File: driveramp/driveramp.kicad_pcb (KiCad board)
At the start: 2 copper layers, 109 x 79 mm, 62 parts, among them J1 SMA, J2 SMA, P1 FAULT, P2 CONN_2, T1 MABA-011002, T2 2x Fair-Rite 2843006802, coax, U1 LM2936HVBMA-5.0, U2 MRFE6VP100H, U3 LM317HV

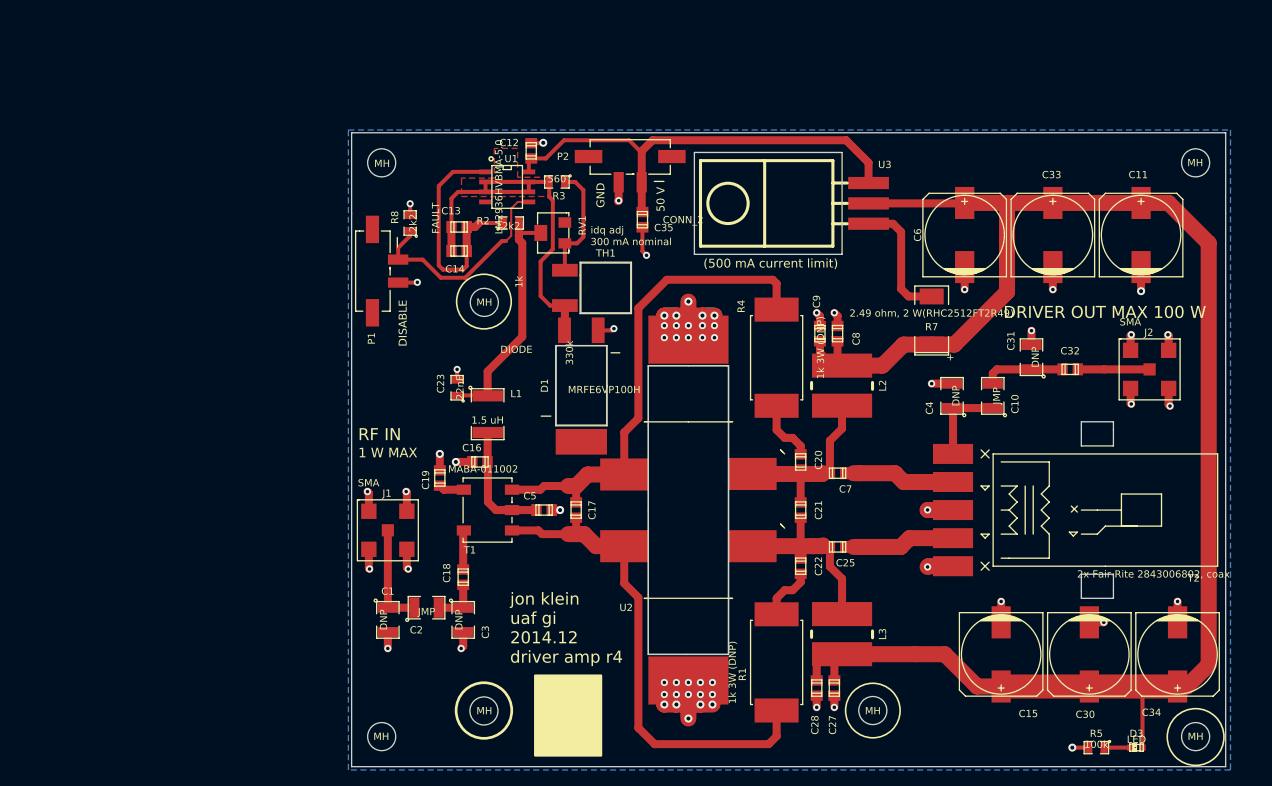
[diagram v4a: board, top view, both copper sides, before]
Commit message: added libraries for r5 driver amp - connectors, mounting holes. changed switch due to availability
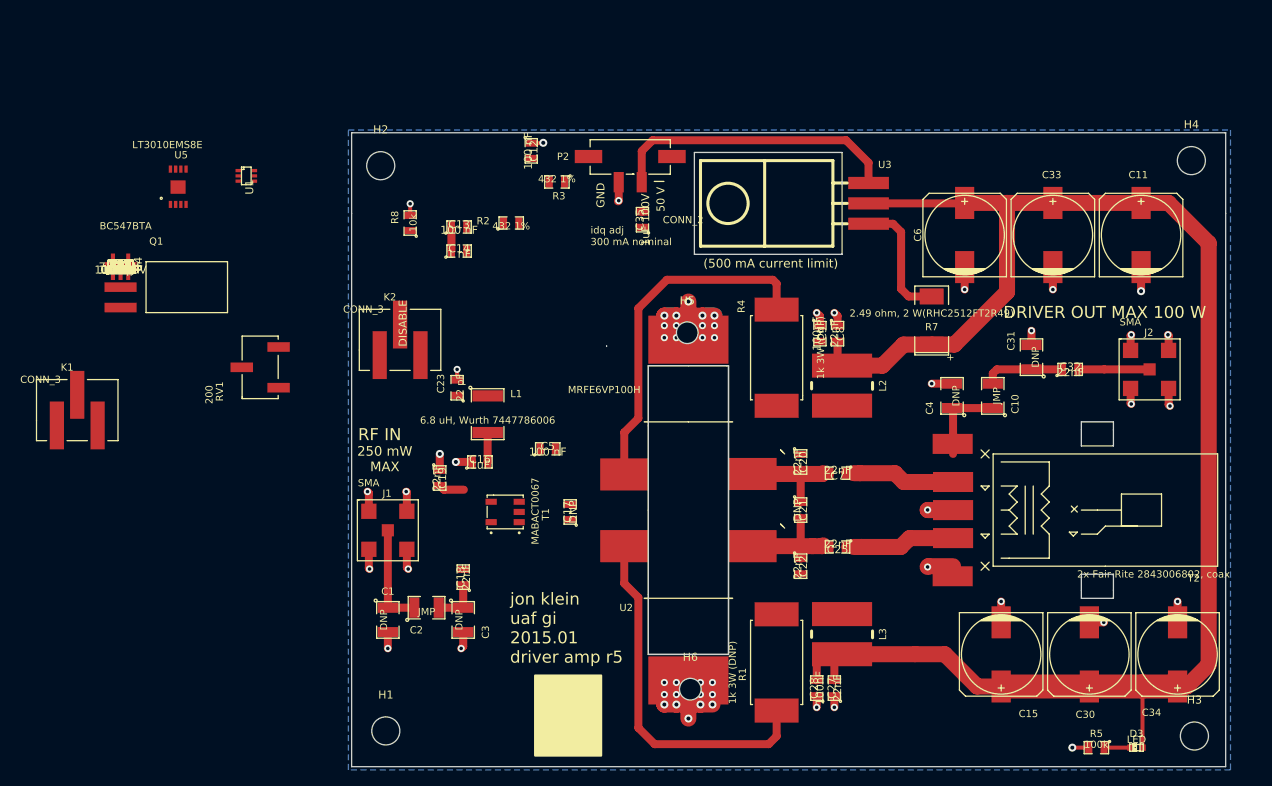
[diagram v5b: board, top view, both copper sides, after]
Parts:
- removed D1: DIODE, local:DUAL_DIODE
- removed MH (x7): MountingHole_3-5mm_RevA_Date21Jun2010, Mounting_Holes:MountingHole_3-5mm
- removed P1: FAULT, local:2-1445053-2
- removed TH1: 330k, local:NTC_HSMOUNT
- added C24: 100 pF, SMD_Packages:SMD-0805, F.Cu at (47.2, 79.7)
- added C26: 10 nF, SMD_Packages:SMD-0805, F.Cu at (47.2, 79.7)
- added C29: 1000 pF, SMD_Packages:SMD-0805, F.Cu at (47.2, 79.7)
- added C36, C39: 100 nF, SMD_Packages:SMD-0805, F.Cu at (47.2, 79.7)
- added C37, C38: 1uF, SMD_Packages:SMD-0805, F.Cu at (47.2, 79.7)
- added C40: 1uF 100V, SMD_Packages:SMD-0805, F.Cu at (47.2, 79.7)
- added H1: MOUNTING_HOLE, Mounting_Holes:MountingHole_3-5mm, F.Cu at (80.3, 137.5)
- added H2: MOUNTING_HOLE, Mounting_Holes:MountingHole_3-5mm, F.Cu at (79.6, 67.1)
- added H3: MOUNTING_HOLE, Mounting_Holes:MountingHole_3-5mm, F.Cu at (181.1, 138.2)
- added H4: MOUNTING_HOLE, Mounting_Holes:MountingHole_3-5mm, F.Cu at (180.7, 66.4)
- added H5: MOUNTING_HOLE, Mounting_Holes:MountingHole_2-7mm, F.Cu at (117.9, 87.9)
- added H6: MOUNTING_HOLE, Mounting_Holes:MountingHole_2-7mm, F.Cu at (118.2, 132.3)
- added K1: CONN_3, localconn:3-647166-3, F.Cu at (41.8, 97.5)
- added K2: CONN_3, localconn:3-647166-3, F.Cu at (82.0, 88.8)
- added Q1: BC547BTA, local:TO92SMDSENSE, F.Cu at (47.2, 79.7)
- added R10: 2k 1%, SMD_Packages:SMD-0603, F.Cu at (47.2, 79.7)
- added R11: 1.1k 1%, SMD_Packages:SMD-0603, F.Cu at (47.2, 79.7)
- added R12: 5.11k 1%, SMD_Packages:SMD-0603, F.Cu at (47.2, 79.7)
- added R13: 909 1%, SMD_Packages:SMD-0603, F.Cu at (47.2, 79.7)
- added R14: 10k 1%, SMD_Packages:SMD-0603, F.Cu at (47.2, 79.7)
- added R15: 1.5, SMD_Packages:SMD-0603, F.Cu at (47.2, 79.7)
- added R16: 5.1, SMD_Packages:SMD-0603, F.Cu at (47.2, 79.7)
- added R17, R18: DNP, SMD_Packages:SMD-0805, F.Cu at (47.2, 79.7)
- added R19: 20, SMD_Packages:SMD-0603, F.Cu at (47.2, 79.7)
- added R20: 52.3K 1%, SMD_Packages:SMD-0603, F.Cu at (47.2, 79.7)
- added R21: 10K 1%, SMD_Packages:SMD-0603, F.Cu at (47.2, 79.7)
- added R22: 10k, SMD_Packages:SMD-0603, F.Cu at (47.2, 79.7)
- added R23: 6.2 k, SMD_Packages:SMD-0603, F.Cu at (47.2, 79.7)
- added R6: 75 1%, SMD_Packages:SMD-0603, F.Cu at (47.2, 79.7)
- added R9: 9.1k, SMD_Packages:SMD-0603, F.Cu at (47.2, 79.7)
- added U4: 7321MF, SMD_Packages:SOT-23-5, F.Cu at (47.2, 79.7)
- added U5: LT3010EMS8E, local:MSOP8-EP, F.Cu at (54.4, 69.7)
- C12: value 100nF 50V -> 100 nF; footprint Capacitors_SMD:c_0805 -> SMD_Packages:SMD-0805
- C13: value 2.2uF -> 100 nF; footprint Capacitors_SMD:c_0805 -> SMD_Packages:SMD-0805
- C14: value 22nF -> 1 nF; footprint Capacitors_SMD:c_0805 -> SMD_Packages:SMD-0805
- C16: value 100nF -> 1uF; footprint Capacitors_SMD:c_0805 -> SMD_Packages:SMD-0805
- C17, C18, C19, C20, C21, C22, C25, C27, C28, C32, C35, C7, C8, C9: footprint Capacitors_SMD:c_0805 -> SMD_Packages:SMD-0805
- C23: value 22nF -> 22 pF
- C5: value 22nF -> 100 nF; footprint Capacitors_SMD:c_0805 -> SMD_Packages:SMD-0805
- L1: value 1.5 uH -> 6.8 uH, Wurth 7447786006
- R2: value 2k2 -> 432 1%
- R3: value 560 -> 432 1%
- R8: value 2k2 -> 10k
- RV1: value 1k -> 200; footprint local:POT_SMD -> local:3269W
- T1: value MABA-011002 -> MABACT0067; footprint local:MABA-01002 -> local:SM-22
- U1: value LM2936HVBMA-5.0 -> DG9411; footprint SOIC_Packages:SOIC-8_N -> Transistors_SMD:sc70-6
- moved RV1 40.1 mm to (64.6, 92.2)
- moved U1 32.6 mm to (62.9, 68.3)
- moved C5 7.65 mm to (100.5, 102.4), turned to 0 degrees
- moved T1 3.91 mm to (96.9, 110.2)
- moved C17 0.79 mm to (103.3, 110.2), turned to 90 degrees
- turned C32 to 0 degrees
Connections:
- C12 pad 1: /Vconn -> Net-(C12-Pad1)
- C13 pad 2: Net-(C13-Pad2) -> GND
- C14 pad 1: Net-(C13-Pad1) -> Net-(C14-Pad1)
- C14 pad 2: Net-(C13-Pad2) -> GND
- C23 pad 1: Net-(C23-Pad1) -> Net-(C14-Pad1)
- C5 pad 1: Net-(C16-Pad1) -> Net-(C5-Pad1)
- L1 pad 1: Net-(C23-Pad1) -> /Vconn
- L1 pad 2: Net-(C16-Pad1) -> Net-(C40-Pad1)
- R2 pad 1: Net-(C13-Pad1) -> +8V
- R2 pad 2: Net-(C23-Pad1) -> Net-(R2-Pad2)
- R3 pad 1: Net-(R3-Pad1) -> Net-(R2-Pad2)
- R3 pad 2: Net-(C13-Pad2) -> Net-(R3-Pad2)
- R8 pad 1: Net-(P1-Pad1) -> GND
- R8 pad 2: GND -> Net-(R8-Pad2)
- RV1 pad 1: Net-(R3-Pad1) -> Net-(R2-Pad2)
- RV1 pad 2: Net-(C23-Pad1) -> Net-(R10-Pad2)
- RV1 pad 3: (no net) -> Net-(R3-Pad2)
- T1 pad 1: Net-(C17-Pad1) -> Net-(C17-Pad2)
- T1 pad 2: Net-(C16-Pad1) -> Net-(R17-Pad2)
- T1 pad 3: Net-(C17-Pad2) -> Net-(C17-Pad1)
- U1 pad 1: Net-(C13-Pad1) -> Net-(R8-Pad2)
- U1 pad 2: Net-(C13-Pad2) -> Net-(C5-Pad1)
- U1 pad 3: Net-(C13-Pad2) -> GND
- U1 pad 4: (no net) -> Net-(R15-Pad2)
- U1 pad 5: Net-(P1-Pad1) -> Net-(R16-Pad2)
- U1 pad 6: Net-(C13-Pad2) -> Net-(C14-Pad1)
- U2 pad 1: Net-(C17-Pad2) -> (no net)
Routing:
- net Net-(C13-Pad2): track 48.7 -> 0.00 mm
- net Net-(C23-Pad1): track 30.4 -> 0.00 mm
- net Net-(P1-Pad1): track 27.4 -> 0.00 mm
- net Net-(C13-Pad1): track 30.1 -> 3.00 mm
- net /Vconn: track 61.0 -> 36.5 mm
- net Net-(C17-Pad2): track 64.0 -> 43.6 mm
- net Net-(C17-Pad1): track 62.9 -> 45.1 mm
- net Net-(R3-Pad1): track 14.6 -> 0.00 mm
- net Net-(C16-Pad1): track 15.2 -> 2.05 mm, vias 0 -> 1
- net Net-(C21-Pad1): track 30.1 -> 18.6 mm
- net GND: track 203.1 -> 193.4 mm, vias 65 -> 52
- net VDD: track 209.9 -> 200.7 mm, vias 0 -> 4
- net Net-(C25-Pad2): track 14.9 -> 7.47 mm
- net Net-(C7-Pad2): track 14.7 -> 7.39 mm
- net Net-(C22-Pad1): track 6.88 -> 0.00 mm
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- removed copper zone on F.Cu, net Net-(C13-Pad2)
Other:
- outline, holes or cut-outs redrawn
- board text added: "250 mW MAX"
- board text added: "jon klein uaf gi 2015.01 driver amp r5"
- board text removed: "1 W MAX"
- board text removed: "Attach VHS-95 heatsink to bottom"
- board text removed: "jon klein uaf gi 2014.12 driver amp r4"

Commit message: layout on r5
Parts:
- added L4: FERRITE BEAD, SMD_Packages:SMD-0805, F.Cu at (100.5, 67.7)
- R19: footprint SMD_Packages:SMD-0603 -> SMD_Packages:SMD-0805
- R2, R3, R8: footprint SMD_Packages:SM0805 -> SMD_Packages:SMD-0603
- moved Q1 62.8 mm to (109.9, 83.7), turned to 270 degrees
- moved R13 62.2 mm to (109.3, 80.1), turned to 180 degrees
- moved R12 58.4 mm to (105.5, 80.1), turned to 180 degrees
- moved R11 57.7 mm to (104.8, 76.8), turned to 90 degrees
- moved C29 55.9 mm to (99.4, 99.4), turned to 270 degrees
- moved R17 55.1 mm to (99.8, 96.0)
- moved R14 54.8 mm to (102.0, 80.1), turned to 180 degrees
- moved C24 53.9 mm to (97.3, 99.4), turned to 270 degrees
- moved R19 53.5 mm to (100.6, 83.6), turned to 270 degrees
- moved R22 52.6 mm to (98.3, 67.4), turned to 90 degrees
- moved R16 51.9 mm to (96.4, 96.0), turned to 180 degrees
- moved R18 51.4 mm to (98.4, 83.6), turned to 90 degrees
- moved C40 50.5 mm to (95.4, 64.6), turned to 180 degrees
- moved R15 49.9 mm to (93.3, 98.7)
- moved C36 47.5 mm to (94.4, 85.6), turned to 270 degrees
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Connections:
- L1 pad 1: /Vconn -> Net-(L1-Pad1)
- L1 pad 2: Net-(C40-Pad1) -> Net-(L1-Pad2)
- R17 pad 2: Net-(R17-Pad2) -> Net-(L1-Pad1)
- R19 pad 1: Net-(R17-Pad2) -> Net-(C16-Pad1)
- R19 pad 2: Net-(C16-Pad1) -> Net-(L1-Pad1)
- T1 pad 2: Net-(R17-Pad2) -> Net-(L1-Pad2)
- U2 pad 1: (no net) -> Net-(C17-Pad2)
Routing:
- net +8V: track 0.00 -> 72.3 mm, vias 0 -> 5
- net GND: track 193.4 -> 156.3 mm, vias 52 -> 70
- net Net-(L1-Pad1): track 0.00 -> 23.8 mm
- net Net-(C13-Pad1): track 3.00 -> 26.0 mm
- net Net-(K2-Pad2): track 0.00 -> 22.1 mm
- net Net-(C14-Pad1): track 0.00 -> 20.9 mm
- net /Vconn: track 36.5 -> 57.0 mm
- net Net-(C16-Pad1): track 2.05 -> 17.7 mm, vias 1 -> 2
- net Net-(C17-Pad1): track 45.1 -> 60.3 mm
- net Net-(C17-Pad2): track 43.6 -> 58.0 mm
- net Net-(C21-Pad1): track 18.6 -> 30.3 mm
- net Net-(C12-Pad1): track 1.52 -> 10.3 mm, vias 1 -> 0
- net Net-(C22-Pad1): track 0.00 -> 7.44 mm
- net Net-(C25-Pad2): track 7.47 -> 14.9 mm
- net Net-(C7-Pad2): track 7.39 -> 14.7 mm
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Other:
- outline, holes or cut-outs redrawn
- net class Default: clearance 0.254 -> 0.18
- rule trace_clearance: 0.254 -> 0.18
- board text added: "T/R"

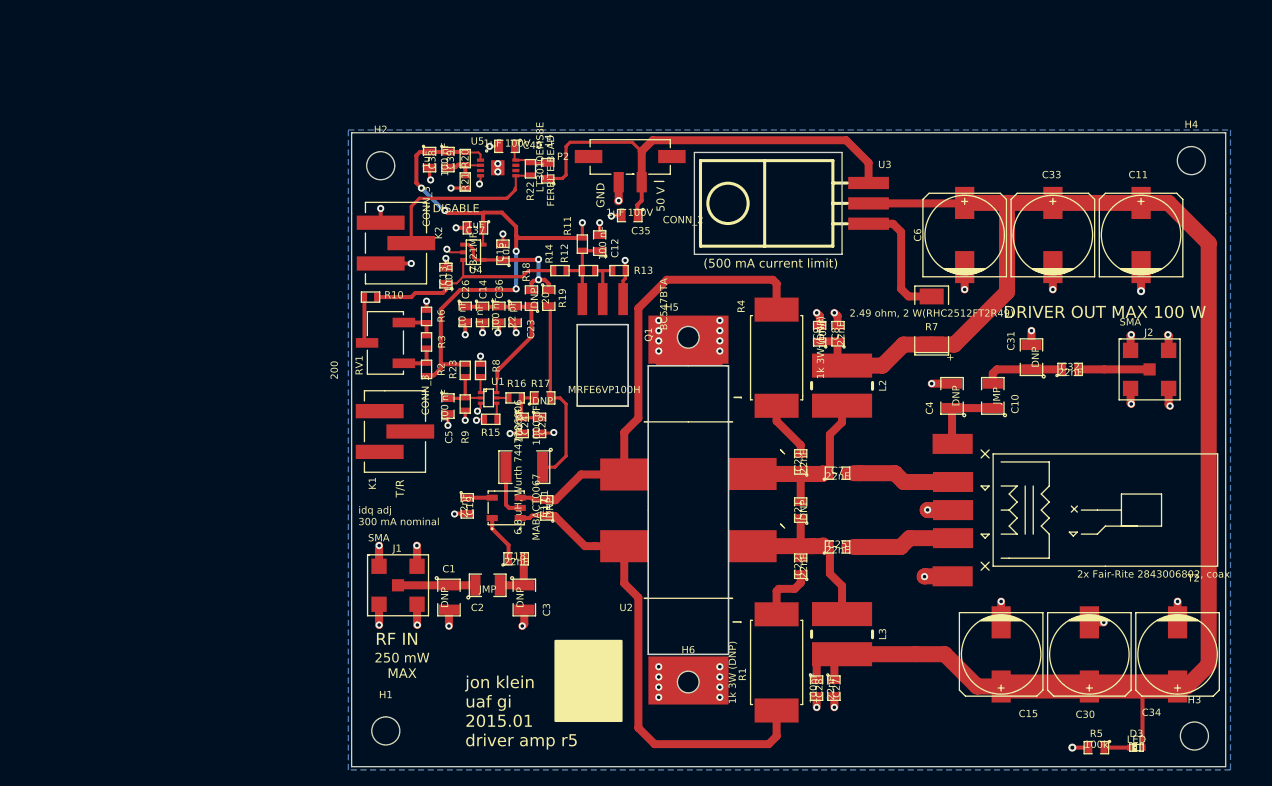
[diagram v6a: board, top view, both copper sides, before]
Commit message: improved manufacturability of driver amp board - increase clearance on transistor heatsink (10 mm width al strip)
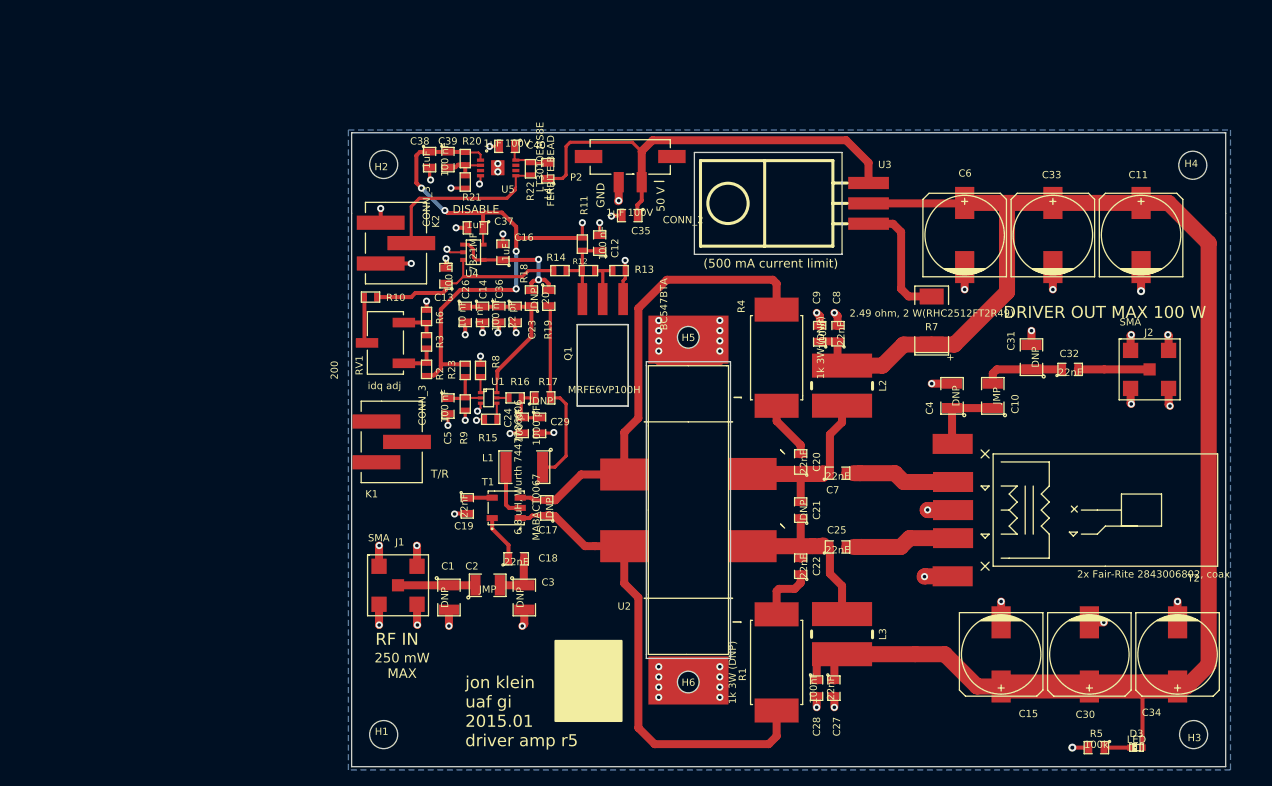
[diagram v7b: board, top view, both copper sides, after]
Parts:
- moved K1 1.36 mm to (81.0, 101.5)
- moved H4 0.61 mm to (180.9, 67.0)
- moved H1 0.53 mm to (80.0, 138.0)
- moved H2 0.40 mm to (80.0, 66.9)
- moved H3 0.20 mm to (181.0, 138.0)
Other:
- outline, holes or cut-outs redrawn
- board text added: "idq adj"
- board text removed: "idq adj 300 mA nominal"

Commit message: finished r5 driver amp..
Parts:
- added D1: DIODE, SMD_Packages:DO-214-AA_SMB, F.Cu at (147.2, 65.5)
- added R24: DNP, SMD_Packages:SMD-0603, F.Cu at (86.1, 96.8)
- C14: value 1 nF -> 1000 pF
- C28, C9: value 100nF -> 100 nF
- L1: value 6.8 uH, Wurth 7447786006 -> 1.5 uH
- moved C35 42.9 mm to (152.8, 65.5), turned to 0 degrees
- moved R7 5.05 mm to (143.8, 84.2), turned to 0 degrees
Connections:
- K1 pad 2: (no net) -> GND
- K1 pad 3: (no net) -> Net-(K1-Pad3)
- L4 pad 1: /Vconn -> VDD
- P2 pad 1: /Vconn -> Net-(D1-Pad1)
- R8 pad 2: Net-(R8-Pad2) -> Net-(K1-Pad3)
- U1 pad 1: Net-(R8-Pad2) -> Net-(K1-Pad3)
- U3 pad 1: Net-(R7-Pad2) -> VDD
- U3 pad 2: VDD -> Net-(R7-Pad2)
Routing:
- net GND: track 156.3 -> 234.7 mm, vias 70 -> 102
- net VDD: track 205.3 -> 273.6 mm, vias 0 -> 10
- net /Vconn: track 57.0 -> 14.4 mm
- net Net-(D1-Pad1): track 0.00 -> 38.3 mm
- net Net-(K1-Pad3): track 0.00 -> 28.0 mm, vias 0 -> 2
- net Net-(R8-Pad2): track 2.01 -> 0.00 mm
- net Net-(C5-Pad1): track 6.85 -> 8.78 mm
- net +8V: track 72.3 -> 70.4 mm, vias 5 -> 4
- net Net-(R7-Pad2): track 15.8 -> 17.3 mm
- added copper zone on F.Cu, net GND
